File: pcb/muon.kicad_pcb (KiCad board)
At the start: 2 copper layers, 57 x 59 mm, 33 parts, among them J1 Debug Pins, J2 USB_C_Receptacle_USB2.0, SW1 SW_Push, SW2 SW_Push, U1 SRV05-4, U2 AP2112, U3 RP2040, U4 W25Q80DVSSIG, Y1 Crystal_GND24_Small

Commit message: close, but not quite v0.2
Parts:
- removed the REF** at (176.5, 60.5)
- removed the REF** at (130.5, 108.5)
- removed the REF** at (176.5, 108.5)
- added C10: 100n, Capacitor_SMD:C_0402_1005Metric, F.Cu at (136.5, 71.2)
- added C11: 100n, Capacitor_SMD:C_0402_1005Metric, F.Cu at (141.0, 71.2)
- added C12: 1u, Capacitor_SMD:C_0402_1005Metric, F.Cu at (139.3, 57.5)
- added C13: 100n, Capacitor_SMD:C_0402_1005Metric, F.Cu at (140.3, 57.5)
- added C14: 100n, Capacitor_SMD:C_0402_1005Metric, F.Cu at (135.5, 71.2)
- added C15: 100n, Capacitor_SMD:C_0402_1005Metric, F.Cu at (133.5, 71.2)
- added C16: 100n, Capacitor_SMD:C_0402_1005Metric, F.Cu at (134.5, 71.2)
- added C17: 100n, Capacitor_SMD:C_0402_1005Metric, F.Cu at (139.7, 71.7)
- added C18: 100n, Capacitor_SMD:C_0402_1005Metric, F.Cu at (138.7, 71.7)
- added C19: 100n, Capacitor_SMD:C_0402_1005Metric, F.Cu at (144.6, 66.6)
- added C20: 1u, Capacitor_SMD:C_0402_1005Metric, F.Cu at (140.7, 41.7)
- added R6: 27R, Resistor_SMD:R_0402_1005Metric, F.Cu at (137.7, 69.6)
- added R7: 27R, Resistor_SMD:R_0402_1005Metric, F.Cu at (138.8, 69.6)
- added REF**: MountingHole_2.5mm, MountingHole:MountingHole_2.5mm, F.Cu at (129.0, 101.0)
- added REF**: MountingHole_2.5mm, MountingHole:MountingHole_2.5mm, F.Cu at (178.0, 101.0)
- added REF**: MountingHole_2.5mm, MountingHole:MountingHole_2.5mm, F.Cu at (178.0, 59.0)
- added SW3: Reset, Button_Switch_SMD:SW_SPST_PTS810, F.Cu at (127.5, 76.0)
- C6, C7, C8, C9: value 0.1u -> 100nF
- F1: value 150mA -> 500mA
- REF**: value MountingHole_4.3mm_M4 -> MountingHole_2.5mm; footprint MountingHole:MountingHole_4.3mm_M4 -> MountingHole:MountingHole_2.5mm
- moved J1 84.2 mm to (128.0, 63.5), turned to 0 degrees
- moved R1 65.5 mm to (126.0, 69.0)
- moved U2 54.1 mm to (163.5, 63.7)
- moved C3 52.8 mm to (166.1, 64.5), turned to -90 degrees
- moved U4 47.0 mm to (153.5, 72.0)
- moved C2 45.2 mm to (160.5, 65.2), turned to -90 degrees
- moved C4 39.5 mm to (145.7, 62.8), turned to 180 degrees
- moved C5 19.9 mm to (146.7, 57.0), turned to 90 degrees
- moved Y1 15.9 mm to (144.0, 57.4), turned to 0 degrees
- moved C1 15.6 mm to (141.3, 57.5), turned to -90 degrees
- moved C8 5.56 mm to (169.5, 85.1), turned to 90 degrees
- moved C6 4.34 mm to (145.8, 85.1), turned to 90 degrees
- moved C7 2.71 mm to (139.0, 95.1), turned to 90 degrees
- moved C9 2.47 mm to (176.0, 95.0), turned to 90 degrees
- moved REF** 2.12 mm to (129.0, 59.0)
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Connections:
- C6 pad 1: +5V -> /5V_LED
- C7 pad 1: +5V -> /5V_LED
- C8 pad 1: +5V -> /5V_LED
- C9 pad 1: +5V -> /5V_LED
- D1 pad 1: +5V -> /5V_LED
- D2 pad 1: +5V -> /5V_LED
- F1 pad 1: /VBUS_F_ -> /VBUS
- F1 pad 2: /VBUS_ -> /5V_LED
- FB1 pad 1: /VBUS_F_ -> /VBUS_
- FB1 pad 2: +5V -> /5V_LED
- LED1 pad 1: +5V -> /5V_LED
- LED2 pad 1: +5V -> /5V_LED
- R2 pad 1: unconnected-(R2-Pad1) -> /KEYGLOW
- R5 pad 1: unconnected-(R5-Pad1) -> /UNDERGLOW
- U1 pad 5: +5V -> /VBUS_
- U3 pad 1: IOVDD -> +3V3
- U3 pad 10: IOVDD -> +3V3
- U3 pad 19: unconnected-(U3-Pad19) -> GND
- U3 pad 2: unconnected-(U3-Pad2) -> /SW1
- U3 pad 22: IOVDD -> +3V3
- U3 pad 23: DVDD -> +1V1
- U3 pad 3: unconnected-(U3-Pad3) -> /SW2
- U3 pad 33: IOVDD -> +3V3
- U3 pad 40: unconnected-(U3-Pad40) -> /UNDERGLOW
- U3 pad 41: unconnected-(U3-Pad41) -> /KEYGLOW
- U3 pad 42: IOVDD -> +3V3
- U3 pad 43: unconnected-(U3-Pad43) -> +3V3
- U3 pad 44: unconnected-(U3-Pad44) -> +3V3
- U3 pad 45: unconnected-(U3-Pad45) -> +1V1
- U3 pad 46: /D- -> Net-(U3-Pad46)
- U3 pad 47: /D+ -> Net-(U3-Pad47)
- U3 pad 48: unconnected-(U3-Pad48) -> +3V3
- U3 pad 49: IOVDD -> +3V3
- U3 pad 50: DVDD -> +1V1
- U3 pad 51: unconnected-(U3-Pad51) -> /QSPI_3
- U3 pad 52: unconnected-(U3-Pad52) -> /QSPI_CLK
- U3 pad 53: unconnected-(U3-Pad53) -> /QSPI_0
- U3 pad 54: unconnected-(U3-Pad54) -> /QSPI_2
- U3 pad 55: unconnected-(U3-Pad55) -> /QSPI_1
- U3 pad 56: unconnected-(U3-Pad56) -> /QSPI_CS
- U4 pad 1: unconnected-(U4-Pad1) -> /QSPI_CS
- U4 pad 2: unconnected-(U4-Pad2) -> /QSPI_1
- U4 pad 3: unconnected-(U4-Pad3) -> /QSPI_2
- U4 pad 4: unconnected-(U4-Pad4) -> GND
- U4 pad 5: unconnected-(U4-Pad5) -> /QSPI_0
- U4 pad 6: unconnected-(U4-Pad6) -> /QSPI_CLK
- U4 pad 7: unconnected-(U4-Pad7) -> /QSPI_3
- U4 pad 8: unconnected-(U4-Pad8) -> +3V3
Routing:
- net /5V_LED: track 0.00 -> 130.2 mm
- net +3V3: track 0.00 -> 88.2 mm, vias 0 -> 5
- net /SW2: track 0.00 -> 39.1 mm
- net Net-(D1-Pad2): track 0.00 -> 34.1 mm
- net /UNDERGLOW: track 0.00 -> 33.1 mm
- net /SW1: track 0.00 -> 32.7 mm
- net +1V1: track 0.00 -> 26.8 mm, vias 0 -> 4
- net /~{RESET}: track 0.00 -> 25.1 mm, vias 0 -> 1
- net /KEYGLOW: track 0.00 -> 23.1 mm
- net /QSPI_3: track 0.00 -> 22.5 mm, vias 0 -> 2
- net +5V: track 27.4 -> 5.50 mm
- net /D-: track 7.22 -> 29.1 mm, vias 0 -> 2
- net /D+: track 4.72 -> 26.0 mm, vias 0 -> 2
- net /QSPI_CLK: track 0.00 -> 20.8 mm, vias 0 -> 2
- net /QSPI_0: track 0.00 -> 19.7 mm
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- added copper zone on F.Cu, net +3V3
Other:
- board size 57 x 59 mm -> 57 x 50 mm

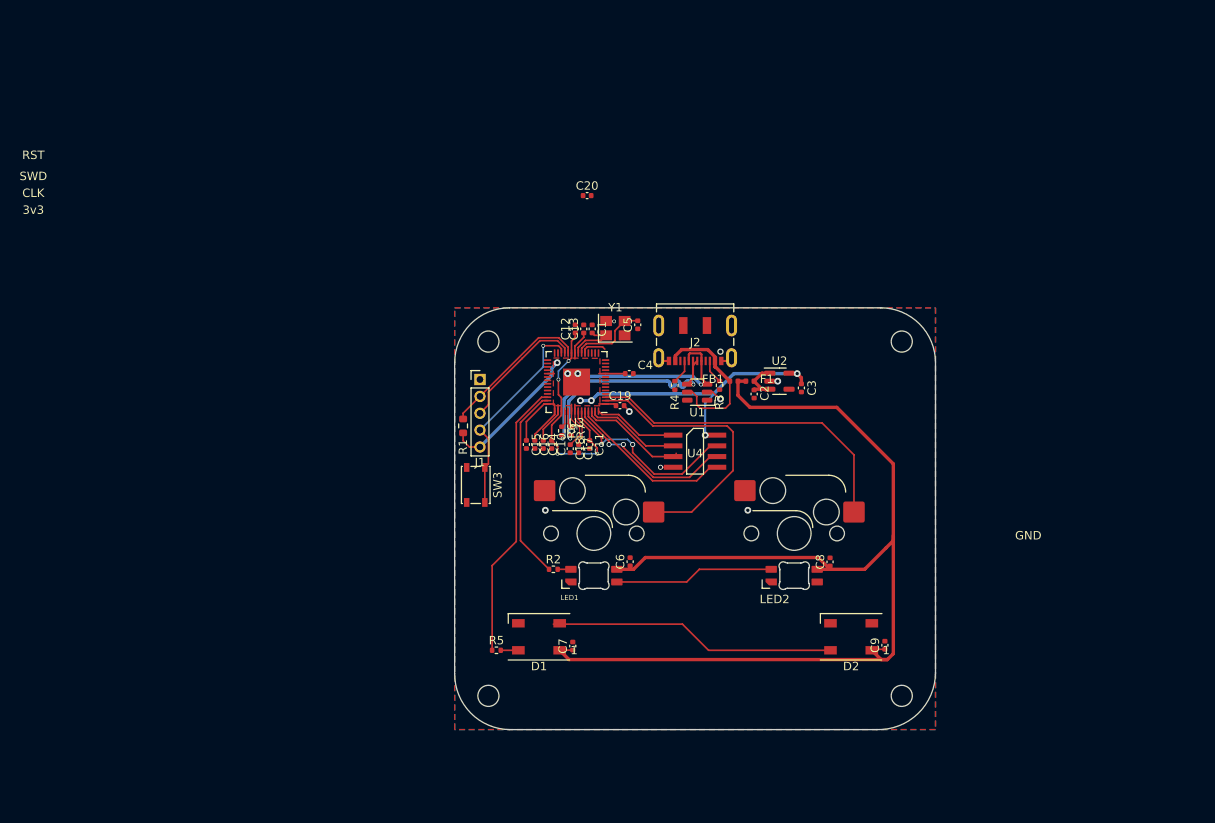
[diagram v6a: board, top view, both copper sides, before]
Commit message: add extra components for debugging and fix arragement of caps
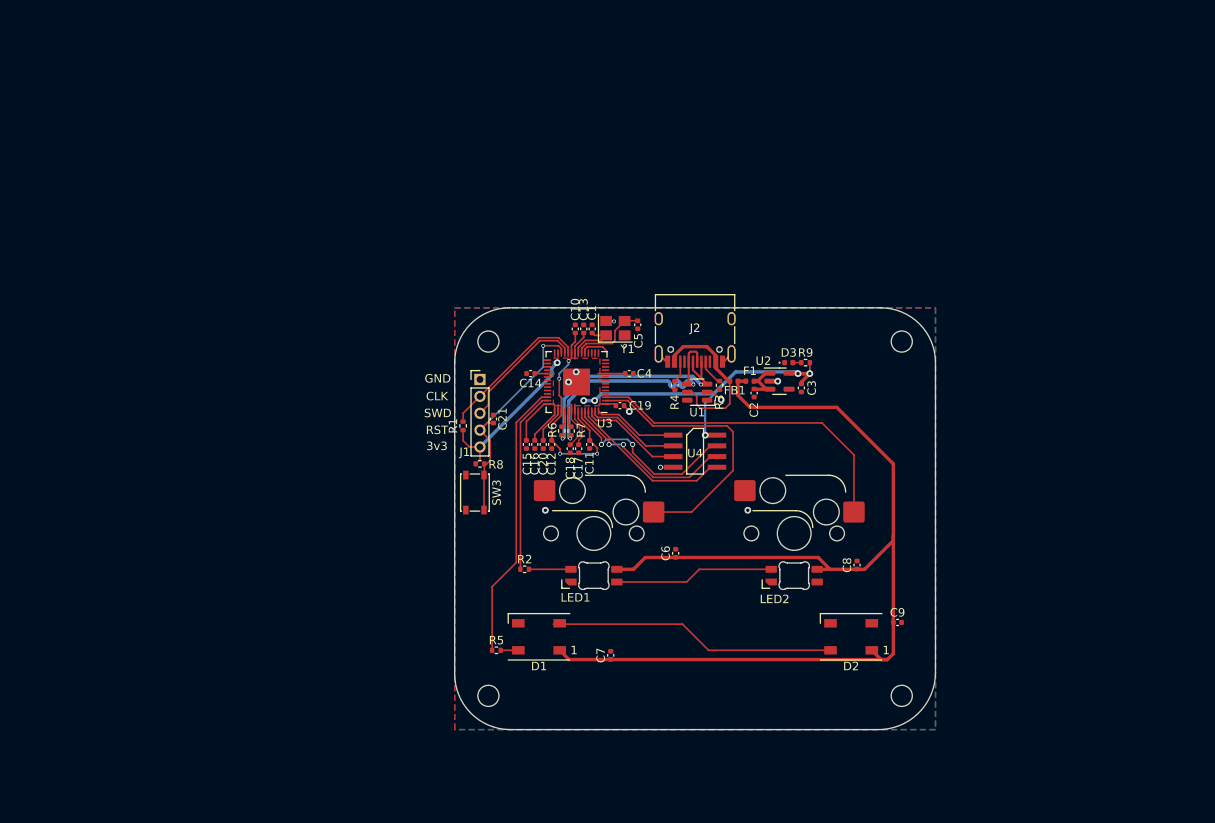
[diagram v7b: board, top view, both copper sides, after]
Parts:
- added C21: 100n, Capacitor_SMD:C_0402_1005Metric, F.Cu at (129.6, 68.2)
- added D3: PWR LED, LED_SMD:LED_0402_1005Metric, F.Cu at (164.6, 61.5)
- added R8: 10k, Resistor_SMD:R_0402_1005Metric, F.Cu at (128.0, 73.5)
- added R9: 1k, Resistor_SMD:R_0402_1005Metric, F.Cu at (166.6, 61.5)
- J2: footprint Connector_USB:USB_C_Receptacle_JAE_DX07S016JA1R1500 -> Connector_USB:USB_C_Receptacle_HRO_TYPE-C-31-M-12
- R1: footprint Resistor_SMD:R_0603_1608Metric -> Resistor_SMD:R_0402_1005Metric
- moved C20 30.0 mm to (135.5, 71.2), turned to -90 degrees
- moved C10 14.0 mm to (139.3, 57.5), turned to 90 degrees
- moved C12 14.0 mm to (136.5, 71.2), turned to -90 degrees
- moved C14 8.53 mm to (134.0, 62.8), turned to 180 degrees
- moved C6 5.49 mm to (151.2, 84.1)
- moved C7 4.63 mm to (143.5, 96.2)
- moved R2 3.40 mm to (133.3, 86.0)
- moved C8 3.22 mm to (172.7, 85.5)
- moved C9 3.09 mm to (177.5, 92.3), turned to 0 degrees
- moved J2 0.91 mm to (153.5, 57.3)
- moved SW3 0.91 mm to (127.4, 76.9)
- moved C2 0.12 mm to (160.5, 65.1)
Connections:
- F1 pad 1: /VBUS -> +5V
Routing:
- net +3V3: track 88.2 -> 97.2 mm, vias 5 -> 6
- net Net-(LED1-Pad3): track 1.56 -> 4.97 mm
- net /~{RESET}: track 25.1 -> 28.3 mm
- net /5V_LED: track 130.2 -> 127.1 mm
- net /D+: track 26.0 -> 28.3 mm
- net /KEYGLOW: track 23.1 -> 21.7 mm
- net /D-: track 29.1 -> 27.8 mm
- net /QSPI_CS: track 11.1 -> 10.0 mm
- net Net-(D3-Pad2): track 0.00 -> 1.00 mm
- net +5V: track 5.50 -> 6.43 mm
- net /VBUS_: track 18.9 -> 19.6 mm
- net GND: vias 9 -> 10

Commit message: v0-2 'release' but not that release-ish
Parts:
- C1, C5: value 5p -> 5pF
- C10, C11, C13, C14, C15, C16, C17, C18, C19, C21: value 100n -> 100nF
- C12, C20: value 1u -> 1uF
- R6, R7: value 27R -> 27
- moved C21 0.50 mm to (130.1, 68.2)
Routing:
- net /~{RESET}: track 28.3 -> 28.8 mm
